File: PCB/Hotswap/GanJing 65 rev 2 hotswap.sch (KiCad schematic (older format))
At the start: 138 parts, among them SW1 EC11_rotary_encoder, U1 Elite-C

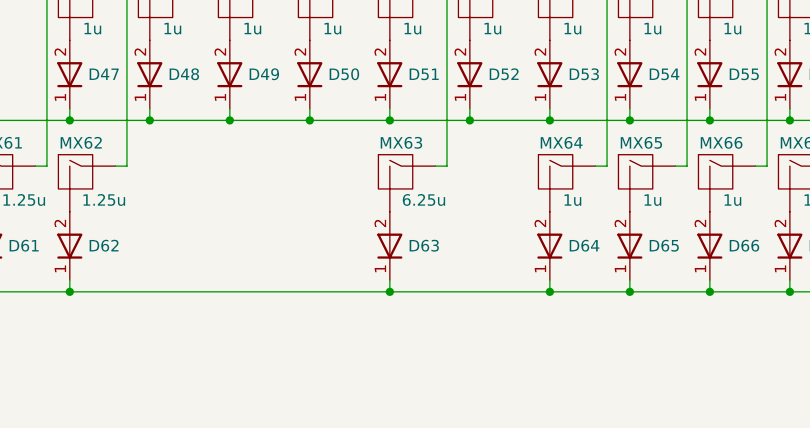
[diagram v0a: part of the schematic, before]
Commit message: Adding split spacebar to hotswap PCB
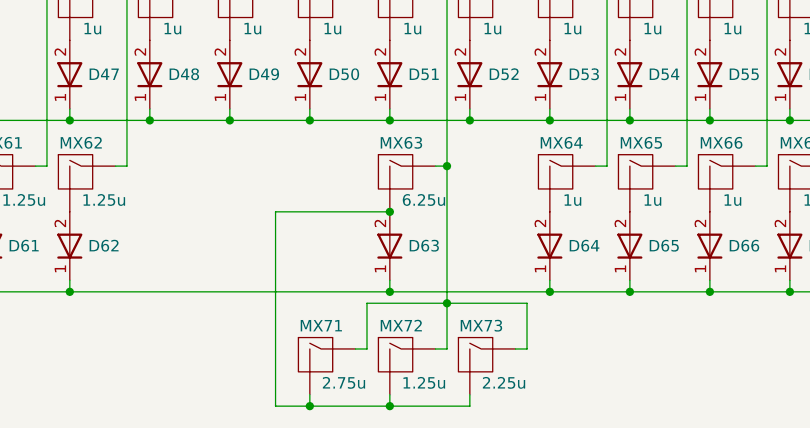
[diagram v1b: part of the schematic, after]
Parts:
- added MX71: MX_2.75u_no_LED_flipped_stabs, GanJing_components:MX_2.75u_no_LED_hotswap_flipped_stabs, symbol GanJing_components:MX_2.75u_no_LED_flipped_stabs
- added MX72: MX_1.25u_no_LED, GanJing_components:MX_1.25u_no_LED_hotswap, symbol GanJing_components:MX_1.25u_no_LED
- added MX73: MX_2.25u_no_LED_flipped_stabs, GanJing_components:MX_2.25u_no_LED_hotswap_flipped_stabs, symbol GanJing_components:MX_2.25u_no_LED_flipped_stabs
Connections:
- net col_7: now also MX71.1 (COL), MX72.1 (COL), MX73.1 (COL)
- net at D63.2, MX63.2 (ROW): now also MX71.2 (ROW), MX72.2 (ROW), MX73.2 (ROW)
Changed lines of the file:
@@
 Wire Wire Line
 	10250 2000 10300 2000
+$Comp
+L GanJing_components:MX_2.75u_no_LED_flipped_stabs MX71
+U 1 1 61BAD7B9
+P 7100 5650
+F 0 "MX71" H 7150 5750 50  0000 C CNN
+F 1 "MX_2.75u_no_LED_flipped_stabs" H 7100 5650 50  0001 C CNN
+F 2 "GanJing_components:MX_2.75u_no_LED_hotswap_flipped_stabs" H 7100 5650 50  0001 C CNN
+F 3 "https://datasheet.octopart.com/MX1A-11NW-Cherry-datasheet-34676.pdf" H 7100 5650 50  0001 C CNN
+F 4 "2.75u" H 7250 5500 50  0000 C CNN "Size"
+	1    7100 5650
+	1    0    0    -1
+$EndComp
+$Comp
+L GanJing_components:MX_2.25u_no_LED_flipped_stabs MX73
+U 1 1 61BADF1C
+P 7800 5650
+F 0 "MX73" H 7850 5750 50  0000 C CNN
+F 1 "MX_2.25u_no_LED_flipped_stabs" H 7800 5650 50  0001 C CNN
+F 2 "GanJing_components:MX_2.25u_no_LED_hotswap_flipped_stabs" H 7800 5650 50  0001 C CNN
+F 3 "https://datasheet.octopart.com/MX1A-11NW-Cherry-datasheet-34676.pdf" H 7800 5650 50  0001 C CNN
+F 4 "2.25u" H 7950 5500 50  0000 C CNN "Size"
+	1    7800 5650
+	1    0    0    -1
+$EndComp
+$Comp
+L GanJing_components:MX_1.25u_no_LED MX72
+U 1 1 61BAF1B1
+P 7450 5650
+F 0 "MX72" H 7500 5750 50  0000 C CNN
+F 1 "MX_1.25u_no_LED" H 7450 5650 50  0001 C CNN
+F 2 "GanJing_components:MX_1.25u_no_LED_hotswap" H 7450 5650 50  0001 C CNN
+F 3 "https://datasheet.octopart.com/MX1A-11NW-Cherry-datasheet-34676.pdf" H 7450 5650 50  0001 C CNN
+F 4 "1.25u" H 7600 5500 50  0000 C CNN "Size"
+	1    7450 5650
+	1    0    0    -1
+$EndComp
+Wire Wire Line
+	7450 5050 6950 5050
+Wire Wire Line
+	6950 5050 6950 5900
+Wire Wire Line
+	6950 5900 7100 5900
+Wire Wire Line
+	7800 5900 7800 5850
+Connection ~ 7450 5050
+Wire Wire Line
+	7450 5850 7450 5900
+Connection ~ 7450 5900
+Wire Wire Line
+	7450 5900 7800 5900
+Wire Wire Line
+	7100 5850 7100 5900
+Connection ~ 7100 5900
+Wire Wire Line
+	7100 5900 7450 5900
+Wire Wire Line
+	7700 4850 7700 5450
+Wire Wire Line
+	7700 5650 7650 5650
+Connection ~ 7700 4850
+Wire Wire Line
+	8000 5650 8050 5650
+Wire Wire Line
+	8050 5650 8050 5450
+Wire Wire Line
+	8050 5450 7700 5450
+Connection ~ 7700 5450
+Wire Wire Line
+	7700 5450 7700 5650
+Wire Wire Line
+	7350 5450 7350 5650
+Wire Wire Line
+	7350 5650 7300 5650
+Wire Wire Line
+	7700 5450 7350 5450
 $EndSCHEMATC
